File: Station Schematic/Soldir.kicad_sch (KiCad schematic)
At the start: 43 parts, among them J1 Conn_01x02, J20 Conn_01x02, J29 Conn_01x02, J30 Conn_01x02, J31 GX12-5M, J32 GX12-5F, Q1 STD10PF06, Q2 BC847B, Q3 BC857B, Q4 BC847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

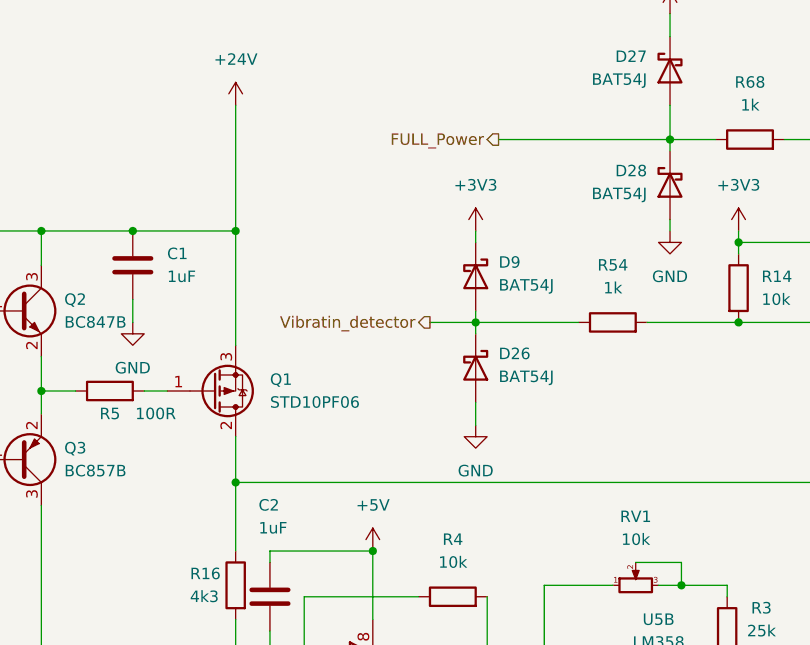
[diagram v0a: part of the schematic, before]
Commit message: PAC was changed
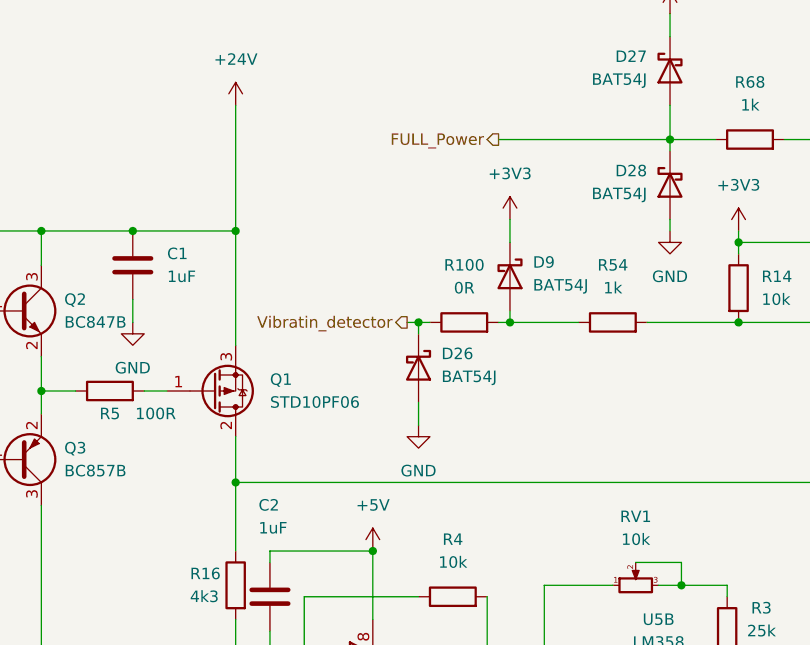
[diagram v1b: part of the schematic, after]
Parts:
- added R100: 0R, Den_Castom_lib:R0 16.128, symbol Device:R
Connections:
- net Vibratin_detector: now also R100.1; no longer D9.2 (A), R54.1
- new net: D9.2 (A), R100.2, R54.1
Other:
- moved on the sheet: D26, D9
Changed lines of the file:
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@@
 	)
 	(junction
+		(at 125.73 58.42)
+		(diameter 0)
+		(color 0 0 0 0)
+	)
+	(junction
 		(at 73.66 48.26)
 		(diameter 0)
@@
 	)
 	(junction
-		(at 121.92 58.42)
+		(at 151.13 49.53)
 		(diameter 0)
 		(color 0 0 0 0)
 	)
 	(junction
-		(at 151.13 49.53)
+		(at 149.86 101.6)
 		(diameter 0)
 		(color 0 0 0 0)
 	)
 	(junction
-		(at 149.86 101.6)
+		(at 144.78 87.63)
 		(diameter 0)
 		(color 0 0 0 0)
 	)
 	(junction
-		(at 144.78 87.63)
+		(at 115.57 58.42)
 		(diameter 0)
 		(color 0 0 0 0)
@@
 	(wire
 		(pts
+			(xy 115.57 67.31) (xy 115.57 69.85)
+		)
+		(stroke
+			(width 0)
+			(type default)
+		)
+	)
+	(wire
+		(pts
 			(xy 241.3 72.39) (xy 252.73 72.39)
 		)
@@
 	(wire
 		(pts
+			(xy 114.3 58.42) (xy 115.57 58.42)
+		)
+		(stroke
+			(width 0)
+			(type default)
+		)
+	)
+	(wire
+		(pts
+			(xy 115.57 58.42) (xy 115.57 59.69)
+		)
+		(stroke
+			(width 0)
+			(type default)
+		)
+	)
+	(wire
+		(pts
+			(xy 124.46 58.42) (xy 125.73 58.42)
+		)
+		(stroke
+			(width 0)
+			(type default)
+		)
+	)
+	(wire
+		(pts
 			(xy 191.77 101.6) (xy 196.85 101.6)
 		)
@@
 	(wire
 		(pts
+			(xy 125.73 57.15) (xy 125.73 58.42)
+		)
+		(stroke
+			(width 0)
+			(type default)
+		)
+	)
+	(wire
+		(pts
 			(xy 29.21 85.09) (xy 33.02 85.09)
 		)
@@
 	(wire
 		(pts
-			(xy 121.92 58.42) (xy 133.35 58.42)
-		)
-		(stroke
-			(width 0)
-			(type default)
-		)
-	)
-	(wire
-		(pts
 			(xy 234.95 33.02) (xy 238.76 33.02)
 		)
@@
 	(wire
 		(pts
-			(xy 121.92 67.31) (xy 121.92 69.85)
-		)
-		(stroke
-			(width 0)
-			(type default)
-		)
-	)
-	(wire
-		(pts
 			(xy 54.61 90.17) (xy 54.61 115.57)
 		)
@@
 	(wire
 		(pts
-			(xy 121.92 58.42) (xy 121.92 59.69)
+			(xy 256.54 25.4) (xy 256.54 27.94)
 		)
 		(stroke
@@
 	(wire
 		(pts
-			(xy 256.54 25.4) (xy 256.54 27.94)
+			(xy 125.73 46.99) (xy 125.73 49.53)
 		)
 		(stroke
@@
 	(wire
 		(pts
-			(xy 121.92 48.26) (xy 121.92 49.53)
-		)
-		(stroke
-			(width 0)
-			(type default)
-		)
-	)
-	(wire
-		(pts
 			(xy 33.02 85.09) (xy 33.02 88.9)
 		)
@@
 	(wire
 		(pts
-			(xy 102.87 101.6) (xy 105.41 101.6)
+			(xy 115.57 58.42) (xy 116.84 58.42)
 		)
 		(stroke
@@
 	(wire
 		(pts
-			(xy 143.51 38.1) (xy 143.51 39.37)
+			(xy 102.87 101.6) (xy 105.41 101.6)
 		)
 		(stroke
@@
 	(wire
 		(pts
-			(xy 102.87 101.6) (xy 102.87 88.9)
+			(xy 143.51 38.1) (xy 143.51 39.37)
 		)
 		(stroke
@@
 	(wire
 		(pts
-			(xy 66.04 64.77) (xy 66.04 73.66)
+			(xy 102.87 101.6) (xy 102.87 88.9)
 		)
 		(stroke
@@
 	(wire
 		(pts
-			(xy 116.84 58.42) (xy 121.92 58.42)
+			(xy 66.04 64.77) (xy 66.04 73.66)
 		)
 		(stroke
@@
 	(wire
 		(pts
-			(xy 142.24 87.63) (xy 144.78 87.63)
+			(xy 125.73 58.42) (xy 133.35 58.42)
 		)
 		(stroke
@@
 	(wire
 		(pts
-			(xy 179.07 38.1) (xy 205.74 38.1)
+			(xy 142.24 87.63) (xy 144.78 87.63)
 		)
 		(stroke
@@
 	(wire
 		(pts
-			(xy 191.77 100.33) (xy 191.77 101.6)
+			(xy 179.07 38.1) (xy 205.74 38.1)
 		)
 		(stroke
@@
 	(wire
 		(pts
-			(xy 54.61 64.77) (xy 55.88 64.77)
+			(xy 191.77 100.33) (xy 191.77 101.6)
 		)
 		(stroke
@@
 	(wire
 		(pts
-			(xy 241.3 69.85) (xy 246.38 69.85)
+			(xy 54.61 64.77) (xy 55.88 64.77)
 		)
 		(stroke
@@
 	(wire
 		(pts
-			(xy 95.25 48.26) (xy 95.25 60.96)
+			(xy 241.3 69.85) (xy 246.38 69.85)
 		)
 		(stroke
@@
 	(wire
 		(pts
-			(xy 121.92 57.15) (xy 121.92 58.42)
+			(xy 95.25 48.26) (xy 95.25 60.96)
 		)
 		(stroke
@@
 	(hierarchical_label "Vibratin_detector"
 		(shape output)
-		(at 116.84 58.42 180)
+		(at 114.3 58.42 180)
 		(fields_autoplaced yes)
 		(effects
@@
 		(lib_name "+3V3_1")
 		(lib_id "power:+3V3")
-		(at 121.92 48.26 0)
+		(at 125.73 46.99 0)
 		(unit 1)
 		(exclude_from_sim no)
@@
 		(fields_autoplaced yes)
 		(property "Reference" "#PWR040"
-			(at 121.92 52.07 0)
+			(at 125.73 50.8 0)
 			(effects
 				(font
@@
 		)
 		(property "Value" "+3V3"
-			(at 121.92 43.18 0)
+			(at 125.73 41.91 0)
 			(effects
 				(font
@@
 		)
 		(property "Footprint" ""
-			(at 121.92 48.26 0)
+			(at 125.73 46.99 0)
 			(effects
 				(font
@@
 		)
 		(property "Datasheet" ""
-			(at 121.92 48.26 0)
+			(at 125.73 46.99 0)
 			(effects
 				(font
@@
 		)
 		(property "Description" "Power symbol creates a global label with name \"+3V3\""
-			(at 121.92 48.26 0)
+			(at 125.73 46.99 0)
 			(effects
 				(font
@@
 	(symbol
 		(lib_id "Diode:BAT54J")
-		(at 121.92 63.5 270)
+		(at 115.57 63.5 270)
 		(unit 1)
 		(exclude_from_sim no)
@@
 		(fields_autoplaced yes)
 		(property "Reference" "D26"
-			(at 124.46 61.9124 90)
+			(at 118.11 61.9124 90)
 			(effects
 				(font
@@
 		)
 		(property "Value" "BAT54J"
-			(at 124.46 64.4524 90)
+			(at 118.11 64.4524 90)
 			(effects
 				(font
@@
 		)
 		(property "Footprint" "Diode_SMD:D_SOD-323F"
-			(at 117.475 63.5 0)
+			(at 111.125 63.5 0)
 			(effects
 				(font
@@
 		)
 		(property "Datasheet" "https://assets.nexperia.com/documents/data-sheet/BAT54J.pdf"
-			(at 121.92 63.5 0)
+			(at 115.57 63.5 0)
 			(effects
 				(font
@@
 		)
 		(property "Description" "30V 200mA Schottky diode, SOD-323F"
-			(at 121.92 63.5 0)
+			(at 115.57 63.5 0)
 			(effects
 				(font
@@
 		(lib_name "GND_2")
 		(lib_id "power:GND")
-		(at 121.92 69.85 0)
+		(at 115.57 69.85 0)
 		(unit 1)
 		(exclude_from_sim no)
@@
 		(fields_autoplaced yes)
 		(property "Reference" "#PWR069"
-			(at 121.92 76.2 0)
+			(at 115.57 76.2 0)
 			(effects
 				(font
@@
 		)
 		(property "Value" "GND"
-			(at 121.92 74.93 0)
+			(at 115.57 74.93 0)
 			(effects
 				(font
@@
 		)
 		(property "Footprint" ""
-			(at 121.92 69.85 0)
+			(at 115.57 69.85 0)
 			(effects
 				(font
@@
 		)
 		(property "Datasheet" ""
-			(at 121.92 69.85 0)
+			(at 115.57 69.85 0)
 			(effects
 				(font
@@
 		)
 		(property "Description" "Power symbol creates a global label with name \"GND\" , ground"
-			(at 121.92 69.85 0)
+			(at 115.57 69.85 0)
 			(effects
 				(font
@@
 	)
 	(symbol
+		(lib_id "Device:R")
+		(at 120.65 58.42 90)
+		(unit 1)
+		(exclude_from_sim no)
+		(in_bom yes)
+		(on_board yes)
+		(dnp no)
+		(fields_autoplaced yes)
+		(property "Reference" "R100"
+			(at 120.65 52.07 90)
+			(effects
+				(font
+					(size 1.27 1.27)
+				)
+			)
+		)
+		(property "Value" "0R"
+			(at 120.65 54.61 90)
+			(effects
+				(font
+					(size 1.27 1.27)
+				)
+			)
+		)
+		(property "Footprint" "Den_Castom_lib:R0 16.128"
+			(at 120.65 60.198 90)
+			(effects
+				(font
+					(size 1.27 1.27)
+				)
+				(hide yes)
+			)
+		)
+		(property "Datasheet" "~"
+			(at 120.65 58.42 0)
+			(effects
+				(font
+					(size 1.27 1.27)
+				)
+				(hide yes)
+			)
+		)
+		(property "Description" ""
+			(at 120.65 58.42 0)
+			(effects
+				(font
+					(size 1.27 1.27)
+				)
+				(hide yes)
+			)
+		)
+		(pin "1"
+		)
+		(pin "2"
+		)
+		(instances
+			(project "Station"
+				(path "/246120ff-a993-4ec9-9427-16a3edd6008f/24bfc0bb-f777-4abc-bcaa-99ab6250b73a"
+					(reference "R100")
+					(unit 1)
+				)
+			)
+		)
+	)
+	(symbol
 		(lib_id "Connector_Generic:Conn_01x02")
 		(at 219.71 62.23 0)
@@
 	(symbol
 		(lib_id "Diode:BAT54J")
-		(at 121.92 53.34 270)
+		(at 125.73 53.34 270)
 		(unit 1)
 		(exclude_from_sim no)
@@
 		(fields_autoplaced yes)
 		(property "Reference" "D9"
-			(at 124.46 51.7524 90)
+			(at 128.27 51.7524 90)
 			(effects
 				(font
@@
 		)
 		(property "Value" "BAT54J"
-			(at 124.46 54.2924 90)
+			(at 128.27 54.2924 90)
 			(effects
 				(font
@@
 		)
 		(property "Footprint" "Diode_SMD:D_SOD-323F"
-			(at 117.475 53.34 0)
+			(at 121.285 53.34 0)
 			(effects
 				(font
@@
 		)
 		(property "Datasheet" "https://assets.nexperia.com/documents/data-sheet/BAT54J.pdf"
-			(at 121.92 53.34 0)
+			(at 125.73 53.34 0)
 			(effects
 				(font
@@
 		)
 		(property "Description" "30V 200mA Schottky diode, SOD-323F"
-			(at 121.92 53.34 0)
+			(at 125.73 53.34 0)
 			(effects
 				(font
